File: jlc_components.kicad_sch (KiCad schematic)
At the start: 75 parts, among them J4 USB_C_Receptacle_USB2.0, Q1 AO3400A, Q2 MMBT5551L, Q3 BC847, Q4 BC857, U1 ADS7828, U1 NE5532, U11 LMV321, U12 REF3040, U14 OPA330xxDBV, U16 OPA2376xxD, U17 ADS1015IDGS, U18 MCP4728, U19 ULN2003A, U2 PCA9575, U2 SN65HVD230, U20 MPU-6050, U21 CD4051B, U22 A4950E, U24 DRV8833PWP, U25 ADF4158, U26 CS4272, U27 TMUX1108PW, U28 AD7616, U29 ADS1015IDGS, U3 DAC7574, U3 XC6206PxxxMR, U30 MCP3425A0T-ECH, U31 AD5593R, U32 AD654JR, U33 XTR111AxDGQ, U34 MPL3115A2, U35 STM32F411CEUx, U36 STM32F446RCTx, U37 STM32F427VGTx, U38 STM32MP151AACx, U39 STM32F030C8Tx, U4 CS4272, U4 LM7321, U4 STM32F103C8Tx, U5 AD8603, U5 NE555D, U6 MCP6002-xSN, U9 WM8731CLSEFL, Y1 Crystal 8MHz

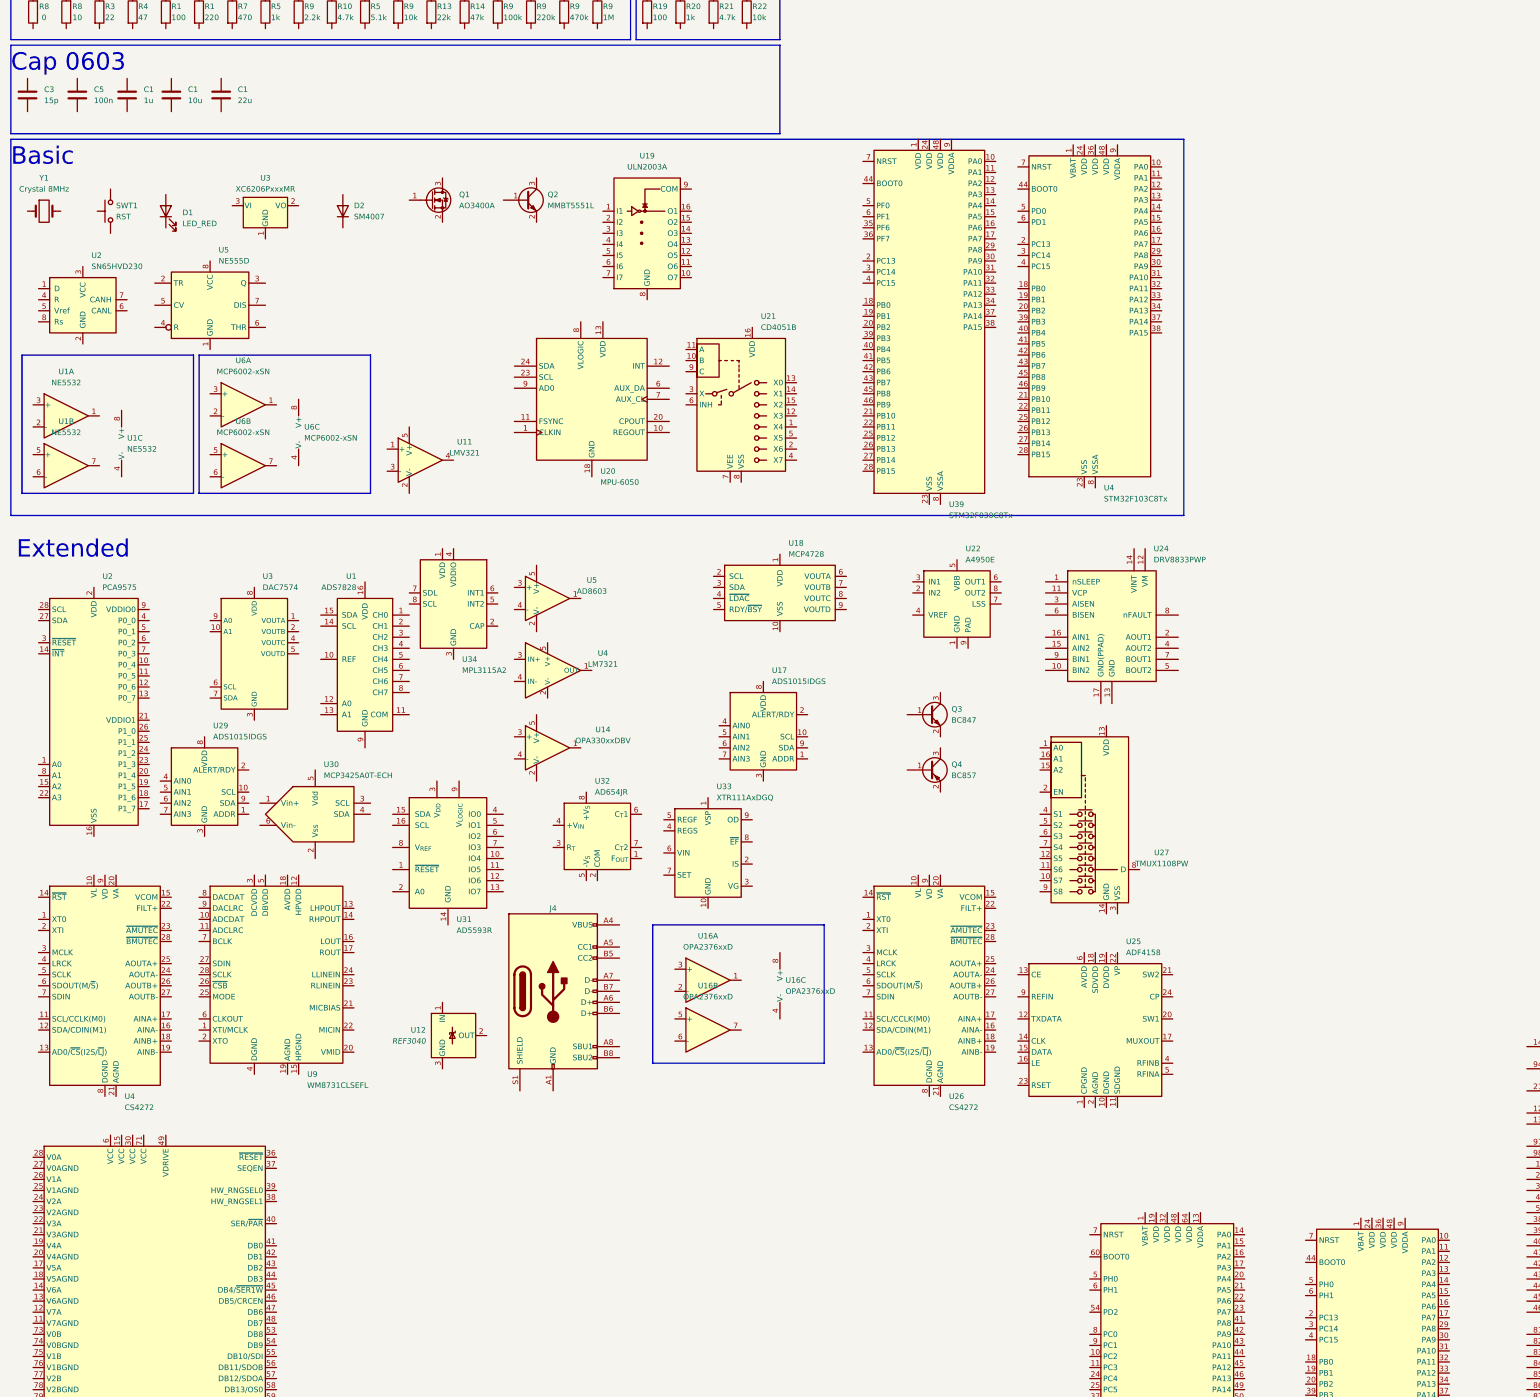
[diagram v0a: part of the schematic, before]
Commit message: added dac7571
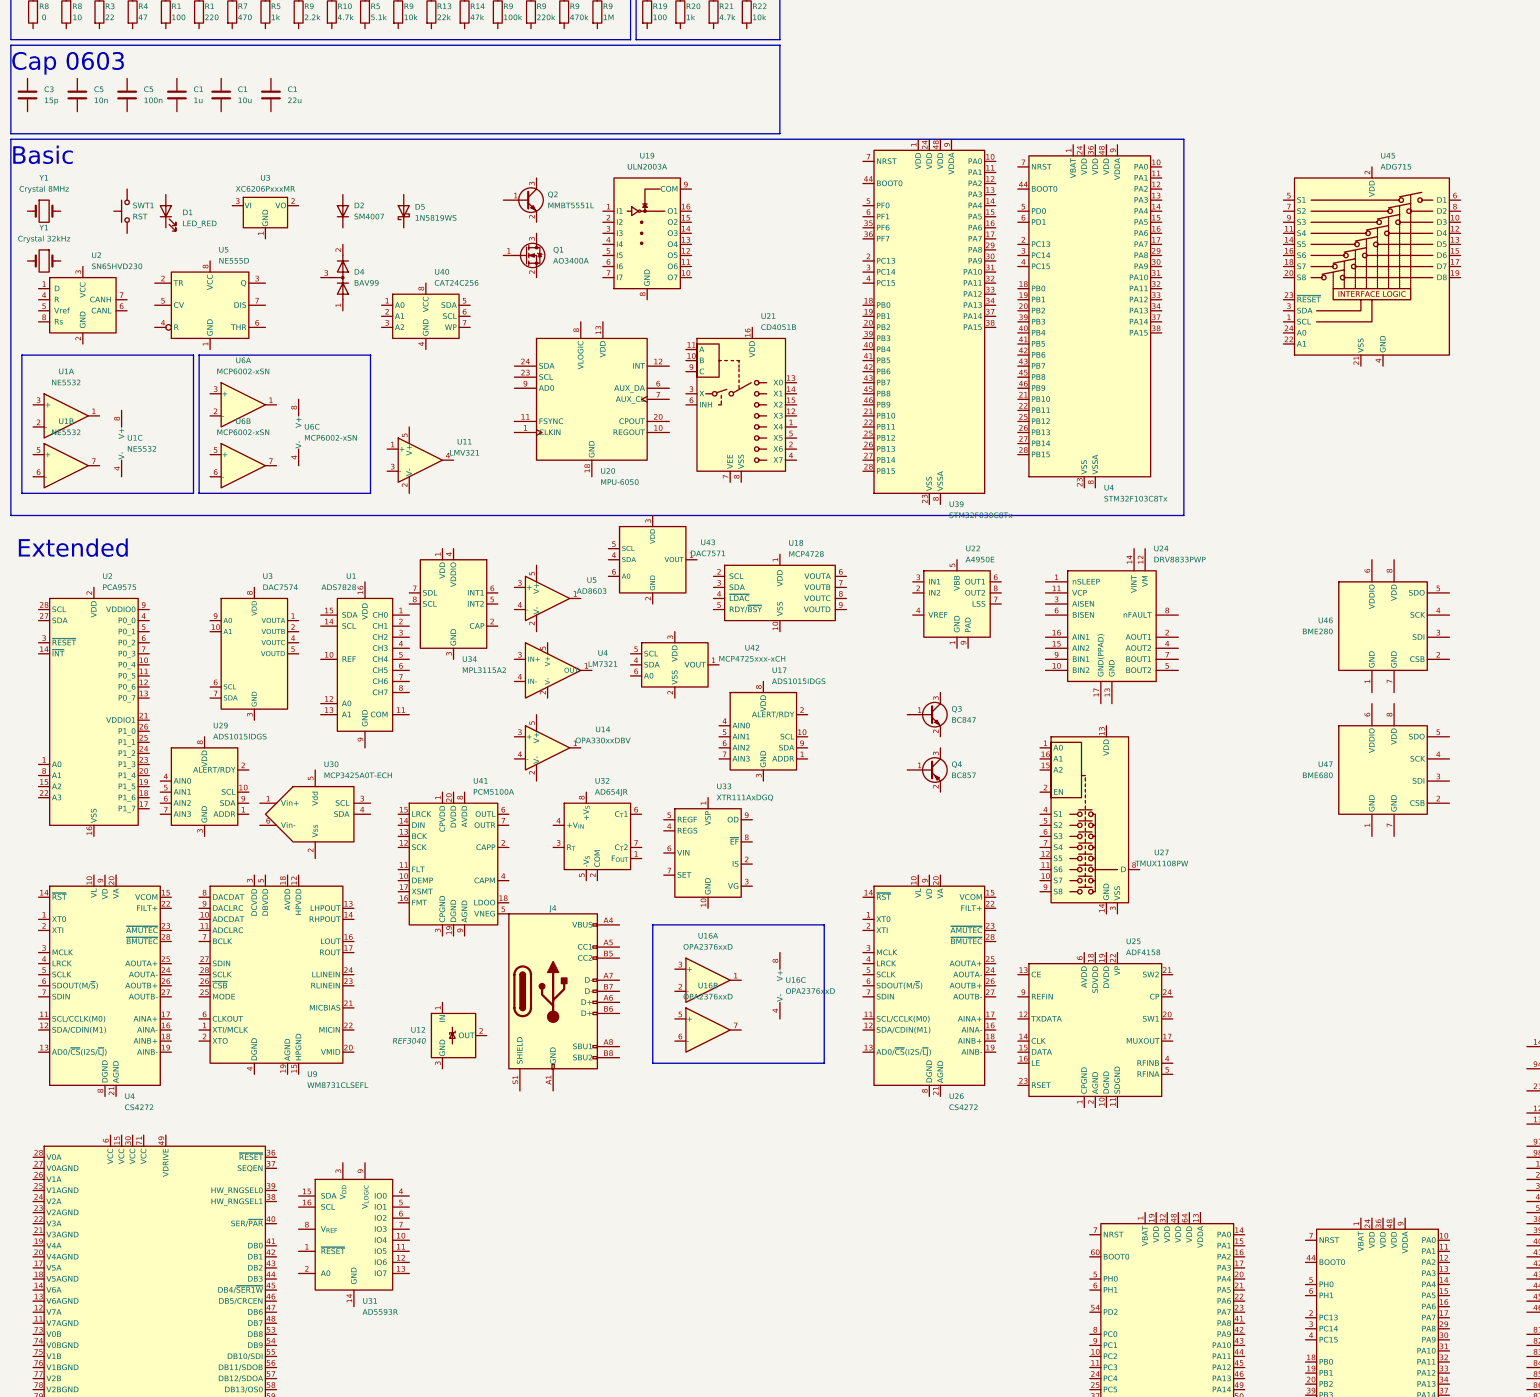
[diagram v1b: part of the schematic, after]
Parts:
- added C5: 10n, Capacitor_SMD:C_0603_1608Metric, symbol Device:C
- added D4: BAV99, Package_TO_SOT_SMD:SOT-23, symbol Diode:BAV99
- added D5: 1N5819WS, Diode_SMD:D_SOD-323, symbol Diode:1N5819WS
- added U40: CAT24C256, Package_SO:SOIC-8_3.9x4.9mm_P1.27mm, symbol Memory_EEPROM:CAT24C256
- added U41: PCM5100A, Package_SO:TSSOP-20_4.4x6.5mm_P0.65mm, symbol Audio:PCM5100A
- added U42: MCP4725xxx-xCH, Package_TO_SOT_SMD:SOT-23-6, symbol Analog_DAC:MCP4725xxx-xCH
- added U43: DAC7571, Package_TO_SOT_SMD:SOT-23-6, symbol yku_symbols:DAC7571
- added U45: ADG715, Package_SO:TSSOP-24_4.4x7.8mm_P0.65mm, symbol Analog_Switch:ADG715
- added U46: BME280, Package_LGA:Bosch_LGA-8_2.5x2.5mm_P0.65mm_ClockwisePinNumbering, symbol Sensor:BME280
- added U47: BME680, Package_LGA:Bosch_LGA-8_3x3mm_P0.8mm_ClockwisePinNumbering, symbol Sensor:BME680
- added Y1: Crystal 32kHz, Crystal:Crystal_SMD_3215-2Pin_3.2x1.5mm, symbol Device:Crystal
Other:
- moved on the sheet: C1, C5, Q1, SWT1, U31

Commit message: added LM8261
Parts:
- added U44: LM8261, Package_TO_SOT_SMD:SOT-23-5, symbol yku_symbols:LM8261
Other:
- moved on the sheet: U14
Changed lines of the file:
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@@
     )
   )
-  (symbol (lib_id "Amplifier_Operational:OPA330xxDBV") (at 137.16 196.85 0) (unit 1)
-    (in_bom yes) (on_board yes) (dnp no) (fields_autoplaced)
-    (property "Reference" "U14" (at 149.86 192.6591 0)
-      (effects (font (size 1.27 1.27)))
-    )
-    (property "Value" "OPA330xxDBV" (at 149.86 195.1991 0)
-      (effects (font (size 1.27 1.27)))
-    )
-    (property "Footprint" "Package_TO_SOT_SMD:SOT-23-5" (at 134.62 201.93 0)
+  (symbol (lib_id "Amplifier_Operational:OPA330xxDBV") (at 120.65 196.85 0) (unit 1)
+    (in_bom yes) (on_board yes) (dnp no) (fields_autoplaced)
+    (property "Reference" "U14" (at 133.35 192.6591 0)
+      (effects (font (size 1.27 1.27)))
+    )
+    (property "Value" "OPA330xxDBV" (at 133.35 195.1991 0)
+      (effects (font (size 1.27 1.27)))
+    )
+    (property "Footprint" "Package_TO_SOT_SMD:SOT-23-5" (at 118.11 201.93 0)
       (effects (font (size 1.27 1.27)) (justify left) hide)
     )
-    (property "Datasheet" "http://www.ti.com/lit/ds/symlink/opa330.pdf" (at 137.16 191.77 0)
-      (effects (font (size 1.27 1.27)) hide)
-    )
-    (property "MPN" "C38649" (at 137.16 196.85 0)
+    (property "Datasheet" "http://www.ti.com/lit/ds/symlink/opa330.pdf" (at 120.65 191.77 0)
+      (effects (font (size 1.27 1.27)) hide)
+    )
+    (property "MPN" "C38649" (at 120.65 196.85 0)
       (effects (font (size 1.27 1.27)) hide)
     )
@@
         )
       )
+    )
+  )
+  (symbol (lib_id "yku_symbols:LM8261") (at 153.67 200.66 0) (unit 1)
+    (in_bom yes) (on_board yes) (dnp no) (fields_autoplaced)
+    (property "Reference" "U44" (at 163.83 187.8204 0)
+      (effects (font (size 1.27 1.27)))
+    )
+    (property "Value" "LM8261" (at 163.83 190.3604 0)
+      (effects (font (size 1.27 1.27)))
+    )
+    (property "Footprint" "Package_TO_SOT_SMD:SOT-23-5" (at 171.45 201.93 0)
+      (effects (font (size 1.27 1.27)) hide)
+    )
+    (property "Datasheet" "https://www.ti.com/lit/ds/symlink/lm8261.pdf" (at 179.07 199.39 0)
+      (effects (font (size 1.27 1.27)) hide)
+    )
+    (property "MPN" "C7968" (at 163.83 192.9004 0)
+      (effects (font (size 1.27 1.27)))
+    )
+    (pin "1")
+    (pin "2")
+    (pin "3")
+    (pin "4")
+    (pin "5")
+    (instances
+      (project "jlc_components"
+        (path "/8e49dde5-50e3-40dd-8040-f3cbad018cf1"
+          (reference "U44") (unit 1)
+        )
+      )
